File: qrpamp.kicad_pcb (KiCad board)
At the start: 2 copper layers, 152.4 x 88.9 mm, 118 parts, among them K1 BAND3_IN, K2 BAND2_IN, K3 BAND1_IN, K4 BAND3_OUT, K5 BAND2_OUT, K6 BAND1_OUT, K7 ANT_RLY, P1 PWR, P2 PWR_SW, P3 SWD, P4 ANT, P5 RADIO, P6 PTT_IN, P7 TP, P8 NAV_BUTTON, Q1 MMBT6427, Q10 MMBF170, Q11 MMBF170, Q3 IRF510, Q4 IRF510, Q6 MMBF170, Q9 MMBF170, SW1 SW_PUSH, T1 8:8, T2 8:8, T3 2:3, T4 12:1, T5 1:12, U1 LM7805, U2 LM3940, U3 LCD-2x16, U4 STM32F401xB/C-LQFP, U5 LTV-356T

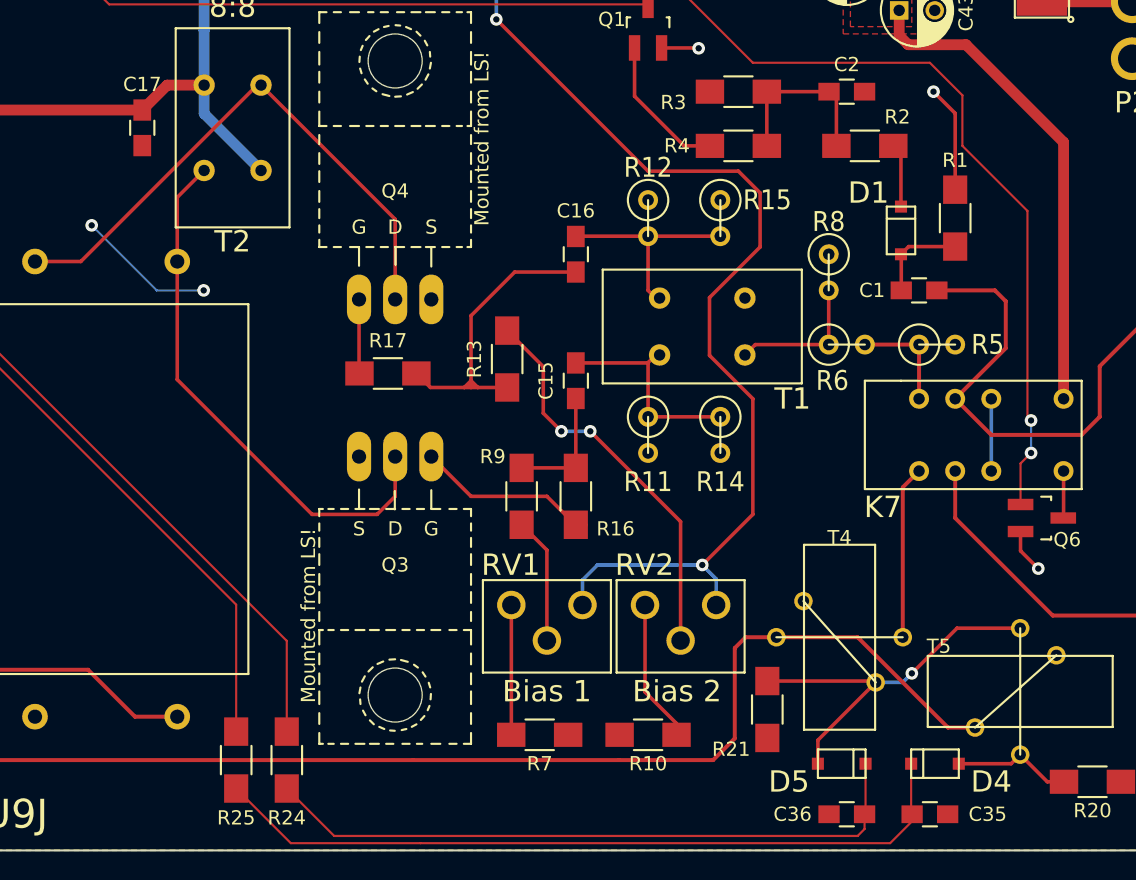
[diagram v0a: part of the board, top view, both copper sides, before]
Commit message: Added a few ground vias, cleaned up some dangling tracks
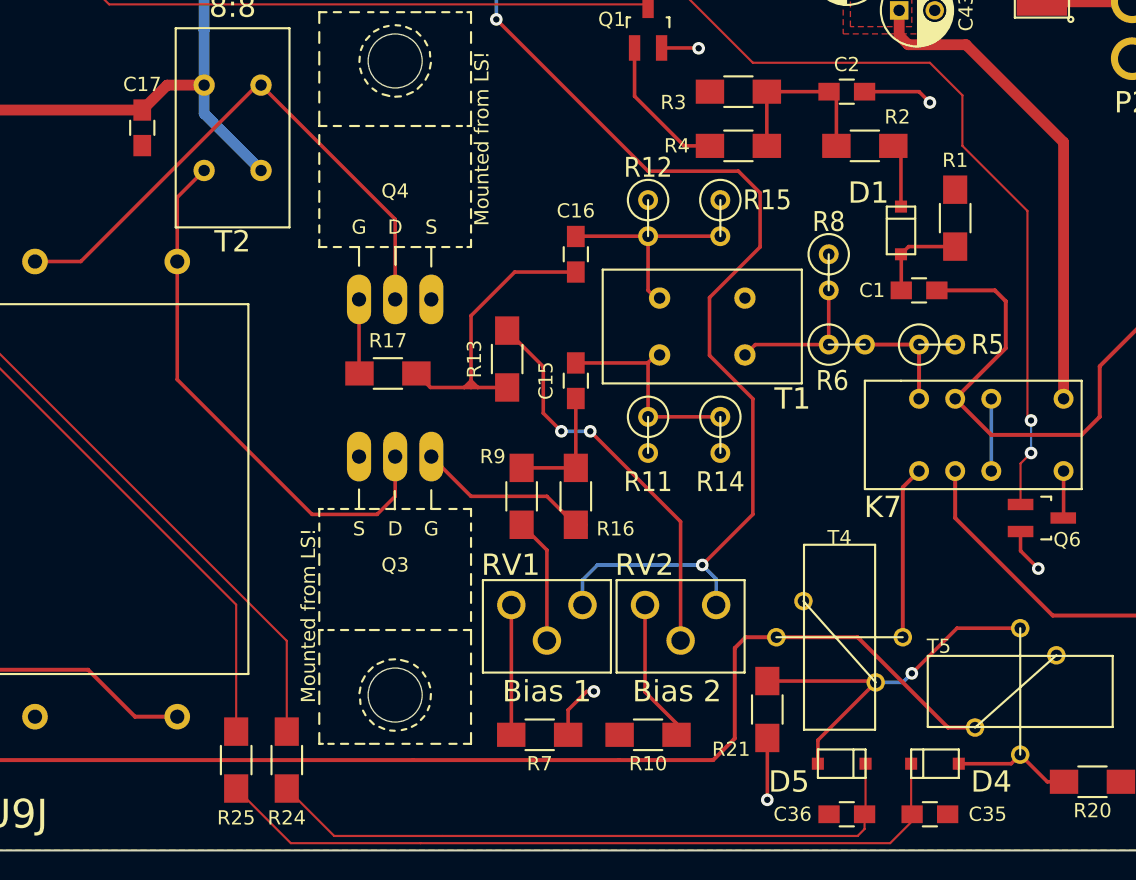
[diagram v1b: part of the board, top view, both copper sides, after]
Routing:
- net (no net): track 9.79 -> 0.00 mm, vias 2 -> 0
- net GND: track 61.5 -> 67.4 mm, vias 13 -> 15

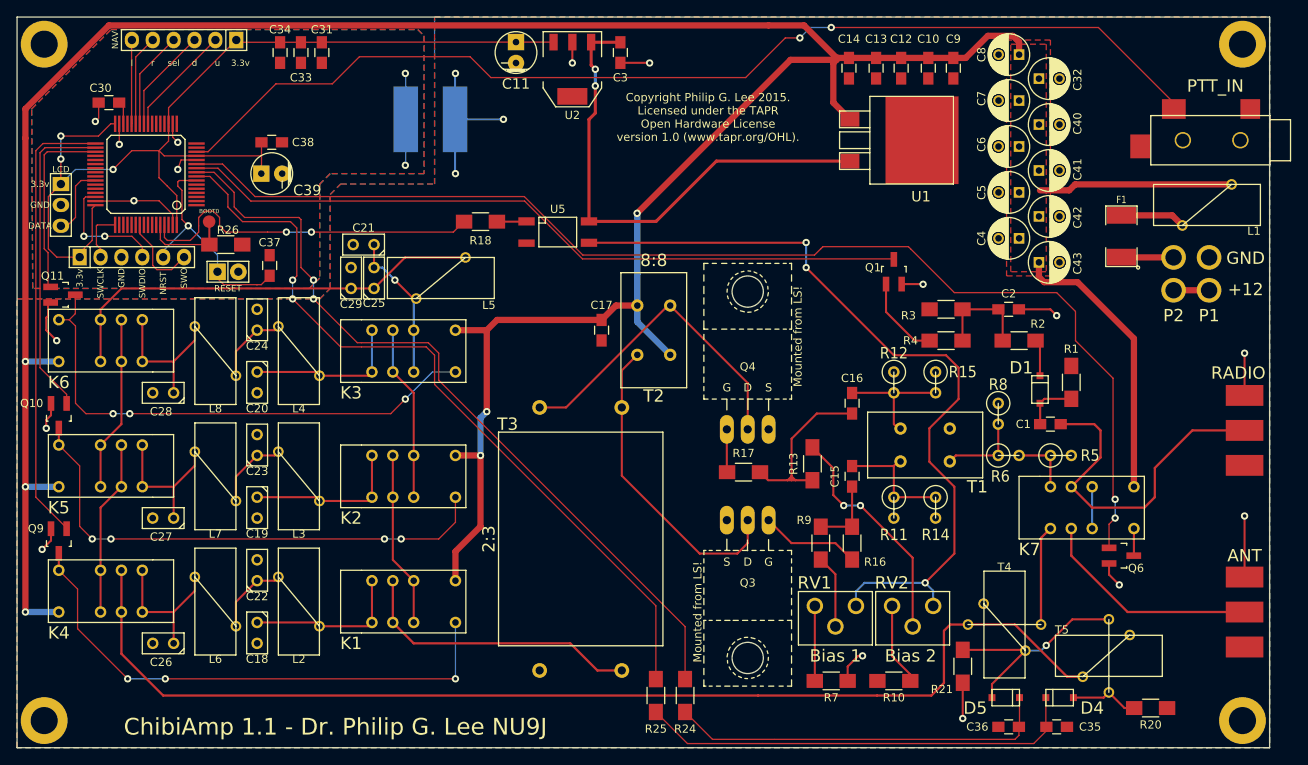
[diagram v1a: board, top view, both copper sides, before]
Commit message: Put MCU decoupling caps on bottom under MCU
This is per the design recommendations in 'PCB Design Guidelines for
Reduced EMI' here: http://www.ti.com/lit/an/szza009/szza009.pdf
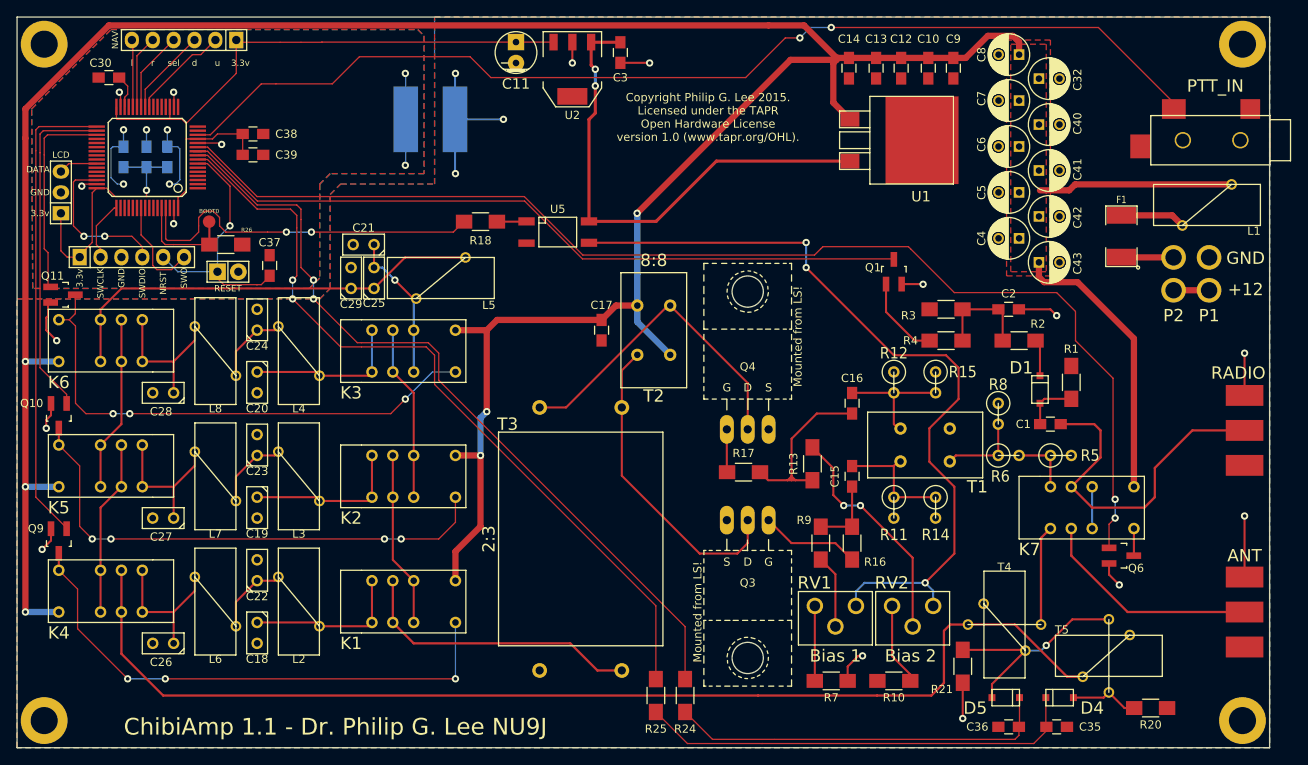
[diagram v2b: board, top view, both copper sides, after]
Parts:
- C31, C33, C34: moved to B.Cu
- C39: footprint Capacitors_ThroughHole:Capacitor5x11RM2.5 -> Capacitors_SMD:C_0805_HandSoldering
- moved C31 24.8 mm to (98.3, 60.2), turned to 90 degrees
- moved C34 22.9 mm to (95.5, 60.2), turned to 90 degrees
- moved C33 20.6 mm to (100.8, 60.2), turned to 90 degrees
- moved C39 3.23 mm to (111.3, 59.9), turned to 0 degrees
- moved C30 3.05 mm to (93.7, 50.5)
- moved C38 2.50 mm to (111.3, 57.4)
- moved U4 2.07 mm to (104.1, 64.0)
- moved U3 1.52 mm to (87.9, 64.5), turned to 90 degrees
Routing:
- net DGND: track 31.2 -> 41.7 mm, vias 7 -> 12
- net +3.3V: track 130.2 -> 120.5 mm, vias 3 -> 1
- net Net-(U3-Pad3): track 9.84 -> 4.76 mm
- net /Microcontroller/SWDIO: track 15.8 -> 20.1 mm
- net /Microcontroller/NRST: track 28.0 -> 31.5 mm
- net /Microcontroller/nav_down: track 14.0 -> 10.6 mm
- net /Microcontroller/nav_left: track 11.2 -> 8.23 mm
- net /Microcontroller/nav_up: track 14.7 -> 12.1 mm
- net /Microcontroller/nav_right: track 11.1 -> 8.93 mm
- net /Microcontroller/nav_select: track 11.9 -> 9.77 mm
- net /Band Filters/bandfilter_3sel: track 56.0 -> 58.1 mm
- net /Microcontroller/mcu_ptt: track 133.6 -> 131.5 mm
- net /Amplifier/amp_on: track 42.8 -> 44.8 mm
- net /Band Filters/bandfilter_2sel: track 39.7 -> 41.6 mm
- net /Band Filters/bandfilter_1sel: track 23.0 -> 24.8 mm
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
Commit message: Added gnd vias to fill in ground pours
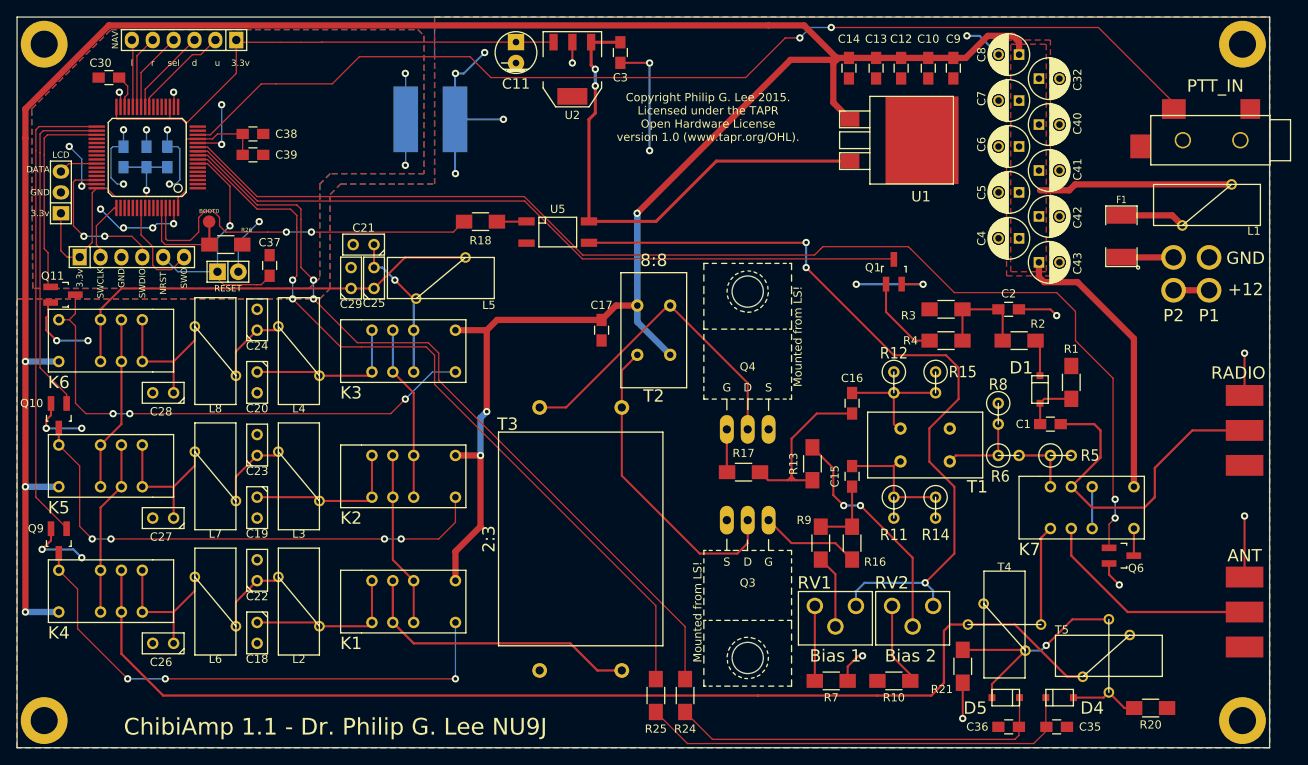
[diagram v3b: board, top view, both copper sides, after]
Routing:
- net GND: track 67.4 -> 108.9 mm, vias 15 -> 22
- net DGND: track 41.7 -> 69.2 mm, vias 12 -> 18
